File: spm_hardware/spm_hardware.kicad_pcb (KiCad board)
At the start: 2 copper layers, 108 x 81 mm, 76 parts, among them J1 Magnet sensor, J2 Floater, J3 MotIn, J4 MotOut, J5 230VAC, J6 USonic sensor, J7 Temp&Humid sensor, J8 Flow sensor, J9 HAL sensor, P1 DIL6, P2 DIL6, P3 DIL6, P4 CONN_01X02, P5 CONN_01X02, P6 CONN_01X02, P7 CONN_01X02, Q1 BS170, Q2 Q_NMOS_DGS, Q3 Q_NMOS_DGS, Q4 Q_NMOS_DGS, T1 Transformer_1P_1S, U1 G3MB-202P, U2 ESP-12E, U3 STM32L432, U4 LTV-817, U5 LTV-817

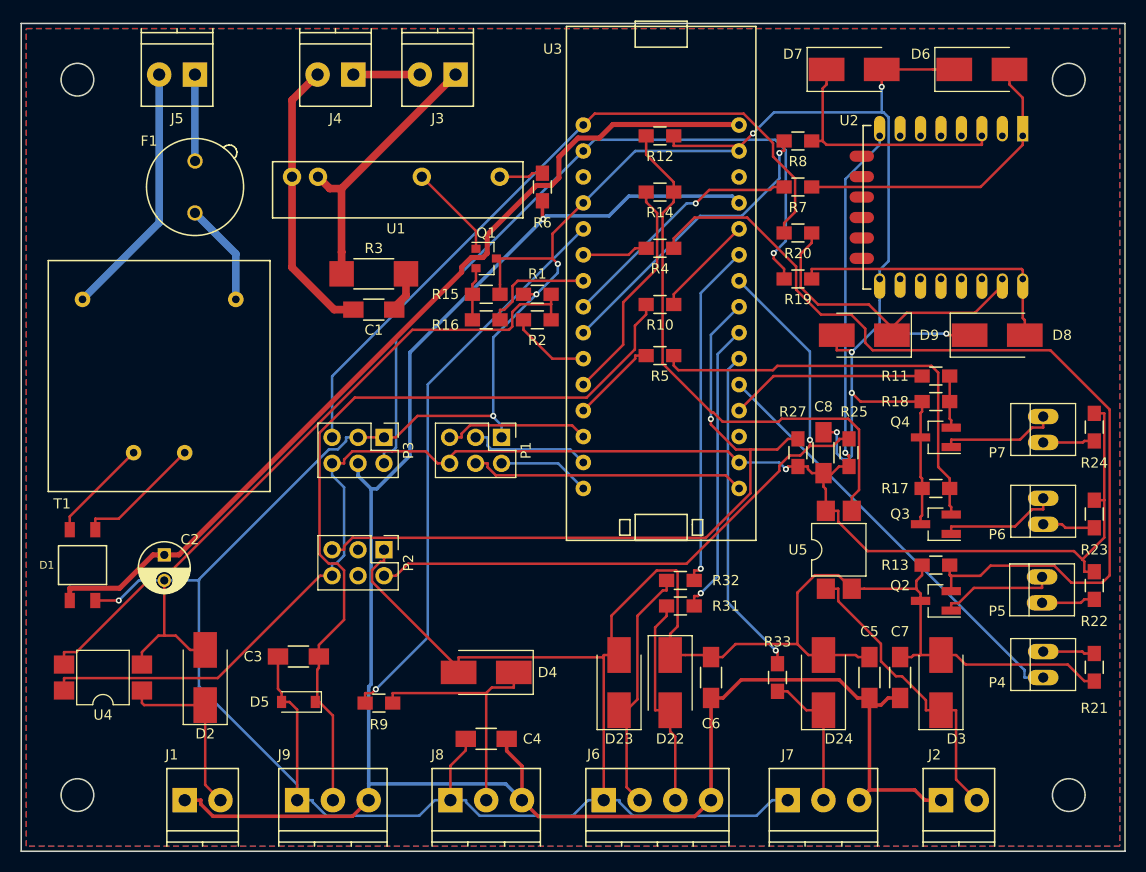
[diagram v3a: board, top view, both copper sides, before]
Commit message: Change UART pins and improve PCB layout
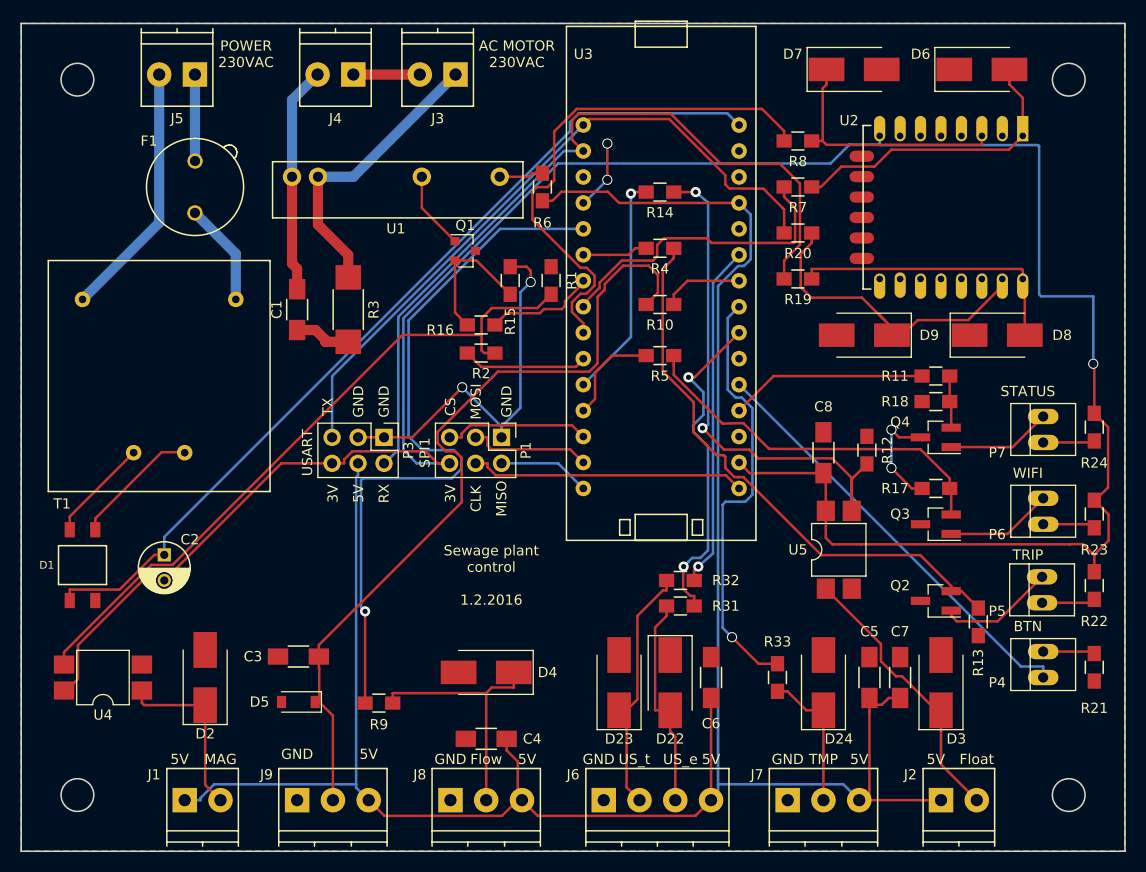
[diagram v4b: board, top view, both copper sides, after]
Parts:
- removed P2: DIL6, Pin_Headers:Pin_Header_Straight_2x03_Pitch2.54mm
- removed R25, R27: R, Resistors_SMD:R_0805_HandSoldering
- moved R12 36.8 mm to (160.7, 90.1), turned to 90 degrees
- moved C1 7.50 mm to (105.0, 76.4), turned to 90 degrees
- moved R13 6.93 mm to (171.6, 106.9), turned to 90 degrees
- moved R2 6.39 mm to (123.0, 80.6)
- moved R3 4.30 mm to (110.0, 76.4), turned to 90 degrees
- moved R15 2.71 mm to (125.8, 73.5), turned to 90 degrees
- moved Q1 2.18 mm to (121.4, 70.6)
- moved R1 1.91 mm to (129.8, 73.5), turned to 90 degrees
- moved R16 0.71 mm to (123.0, 77.9)
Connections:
- U3 pad 20: HAL_Sen -> (no net)
- U3 pad 22: I2C_CLK -> HAL_Sen
- U3 pad 23: I2C_SDA -> TH_Sensor
- U3 pad 25: TH_Sensor -> (no net)
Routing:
- net GND: track 457.8 -> 55.0 mm, vias 10 -> 6
- net I2C_CLK: track 70.4 -> 0.00 mm, vias 1 -> 0
- net I2C_SDA: track 70.3 -> 0.00 mm, vias 1 -> 0
- net +3V3: track 183.1 -> 229.8 mm, vias 2 -> 1
- net Net-(Q2-Pad2): track 90.2 -> 55.6 mm
- net WIFI_EN: track 29.5 -> 51.0 mm, vias 1 -> 0
- net +5V: track 199.2 -> 220.2 mm, vias 1 -> 0
- net Flow_Sen: track 55.6 -> 71.6 mm
- net TH_Sensor: track 32.3 -> 42.5 mm
- net Net-(Q1-Pad2): track 5.19 -> 13.6 mm
- net WIFI_RST: track 24.5 -> 30.7 mm, vias 1 -> 0
- net Net-(C1-Pad2): track 27.6 -> 22.2 mm
- net USART1_RX: track 73.3 -> 78.6 mm, vias 1 -> 0
- net Net-(Q3-Pad2): track 41.9 -> 36.7 mm
- net Mag_Sw: track 8.00 -> 12.3 mm
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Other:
- net class 12V: trace_width 0.5 -> 0.25; via_dia 0.6 -> 1; via_drill 0.4 -> 0.8
- net class 230V: trace_width 0.75 -> 1; via_dia 1.2 -> 1.4; via_drill 0.5 -> 1.2
- net class 5V: trace_width 0.35 -> 0.25; via_dia 0.6 -> 1; via_drill 0.4 -> 0.8
- net class Default: via_dia 0.6 -> 1; via_drill 0.4 -> 0.8
- board text added: "3V"
- board text added: "5V"
- board text added: "AC MOTOR 230VAC"
- board text added: "BTN"
- board text added: "CLK"
- board text added: "CS"
- board text added: "Float"
- board text added: "Flow"
- board text added: "GND"
- board text added: "MAG"
- board text added: "MISO"
- board text added: "MOSI"
- board text added: "POWER 230VAC"
- board text added: "RX"
- board text added: "SPI1"
- board text added: "STATUS"
- board text added: "Sewage plant control 1.2.2016"
- board text added: "TMP"
- board text added: "TRIP"
- board text added: "TX"
- board text added: "USART"
- board text added: "US_e"
- board text added: "US_t"
- board text added: "WIFI"

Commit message: PCB design improved
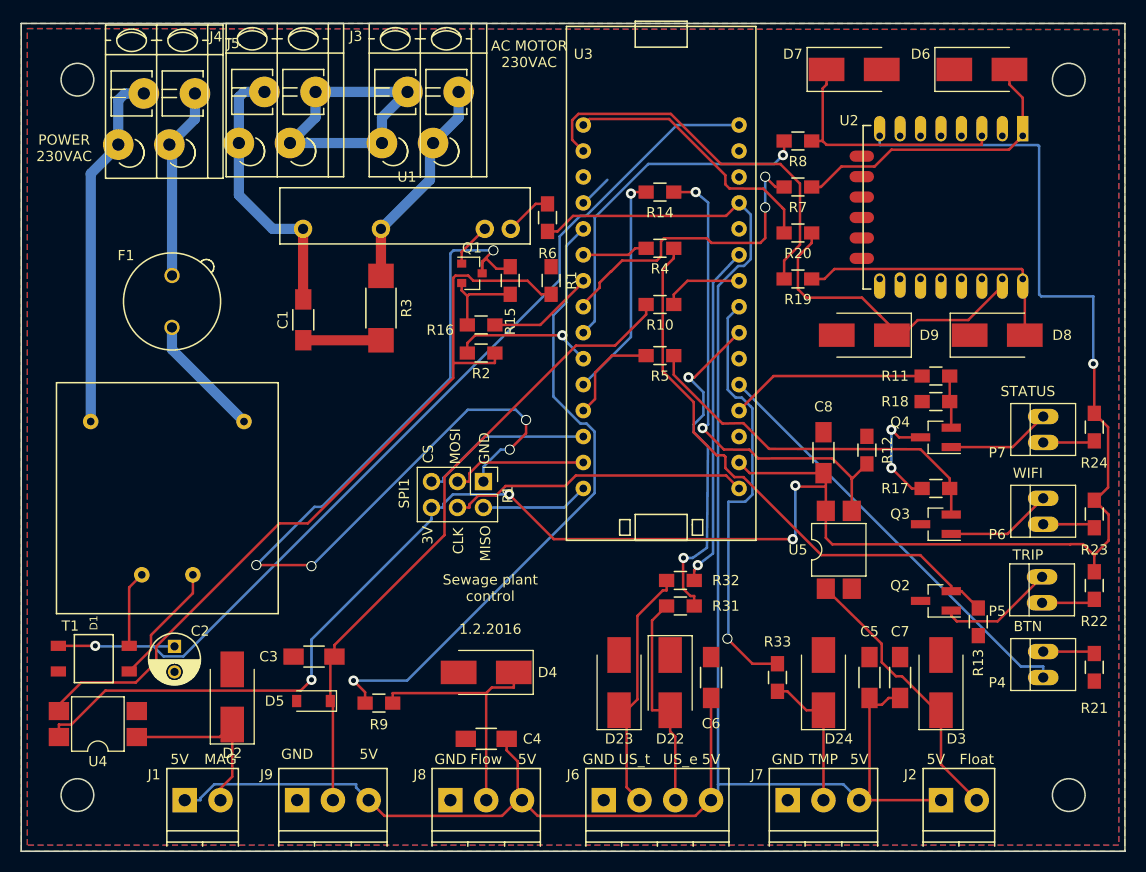
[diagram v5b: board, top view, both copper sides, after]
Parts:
- removed P3: DIL6, Pin_Headers:Pin_Header_Straight_2x03_Pitch2.54mm
- J3, J4, J5: footprint Connectors_Terminal_Blocks:TerminalBlock_Pheonix_PT-3.5mm_2pol -> Connectors_Terminal_Blocks:TerminalBlock_WAGO-804_RM5mm_2pol
- moved U1 22.0 mm to (125.9, 68.5), turned to 180 degrees
- moved T1 12.0 mm to (99.8, 87.3)
- moved F1 11.4 mm to (92.7, 75.6)
- moved D1 9.22 mm to (85.1, 110.5), turned to 270 degrees
- moved C2 9.01 mm to (93.0, 109.3)
- moved P1 4.68 mm to (123.2, 93.2)
- moved U4 4.58 mm to (85.5, 116.9)
- moved J4 4.07 mm to (106.8, 55.1)
- moved D2 3.26 mm to (98.6, 114.3)
- moved R3 3.20 mm to (113.2, 76.2)
- moved R6 3.04 mm to (129.5, 67.4)
- moved Q1 2.29 mm to (122.1, 72.8)
- moved J5 1.85 mm to (95.0, 55.2)
- moved J3 1.73 mm to (120.8, 55.1)
- moved C3 1.53 mm to (106.6, 110.3)
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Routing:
- net GND: track 55.0 -> 105.8 mm, vias 6 -> 7
- net USART1_TX: track 67.1 -> 26.4 mm
- net USART1_RX: track 78.6 -> 38.8 mm
- net +5V: track 220.2 -> 188.6 mm
- net +3V3: track 229.8 -> 203.8 mm, vias 1 -> 5
- net Net-(J3-Pad2): track 6.50 -> 30.1 mm
- net WIFI_EN: track 51.0 -> 34.1 mm, vias 0 -> 1
- net Net-(C3-Pad1): track 80.5 -> 63.6 mm
- net Net-(R1-Pad1): track 67.3 -> 78.6 mm
- net Net-(F1-Pad2): track 8.46 -> 18.7 mm
- net Net-(J5-Pad2): track 25.1 -> 35.3 mm
- net Flow_Sen: track 71.6 -> 62.9 mm
- net Net-(J3-Pad1): track 28.7 -> 21.1 mm
- net +12V: track 87.9 -> 93.1 mm, vias 0 -> 1
- net Net-(Q1-Pad2): track 13.6 -> 8.60 mm
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- added copper zone on B.Cu, net (none)
- added copper zone on F.Cu, net (none)
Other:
- board text removed: "RX"
- board text removed: "TX"
- board text removed: "USART"

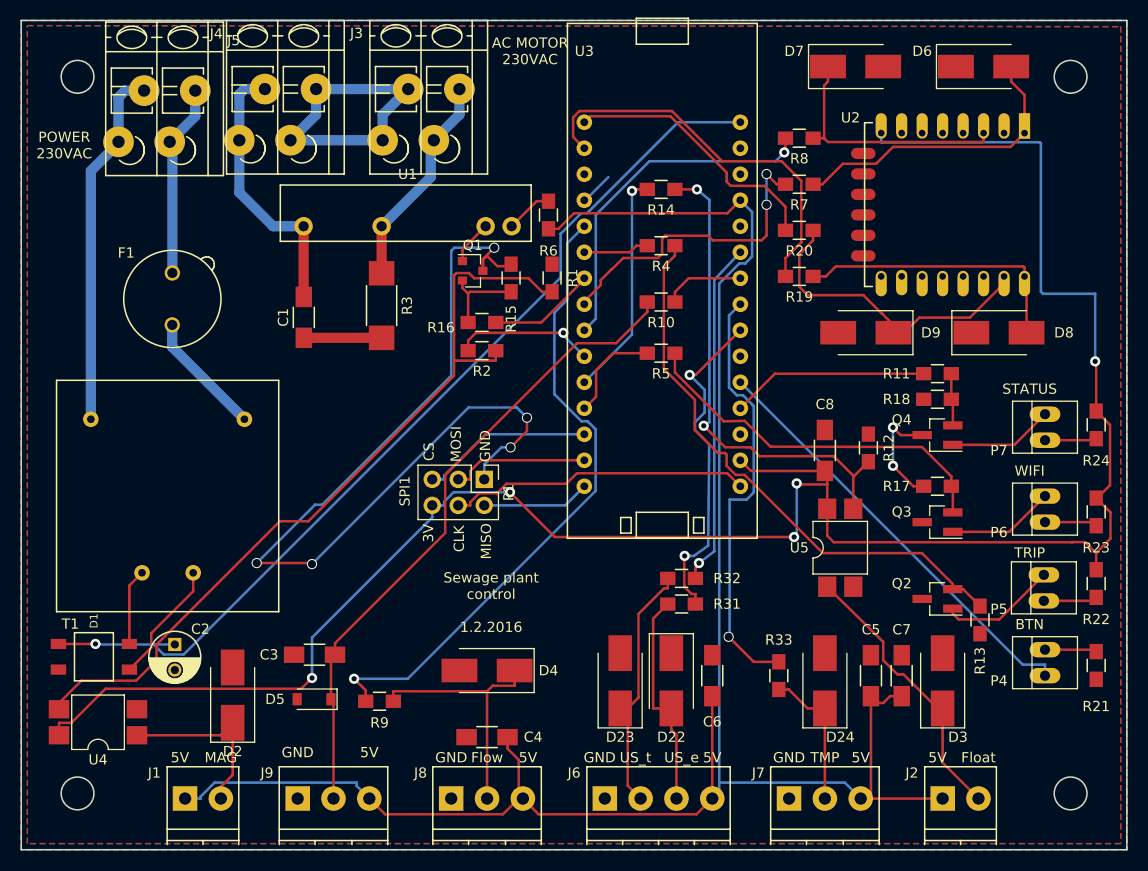
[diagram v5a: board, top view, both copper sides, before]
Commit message: Add custom vias and apply on PCB
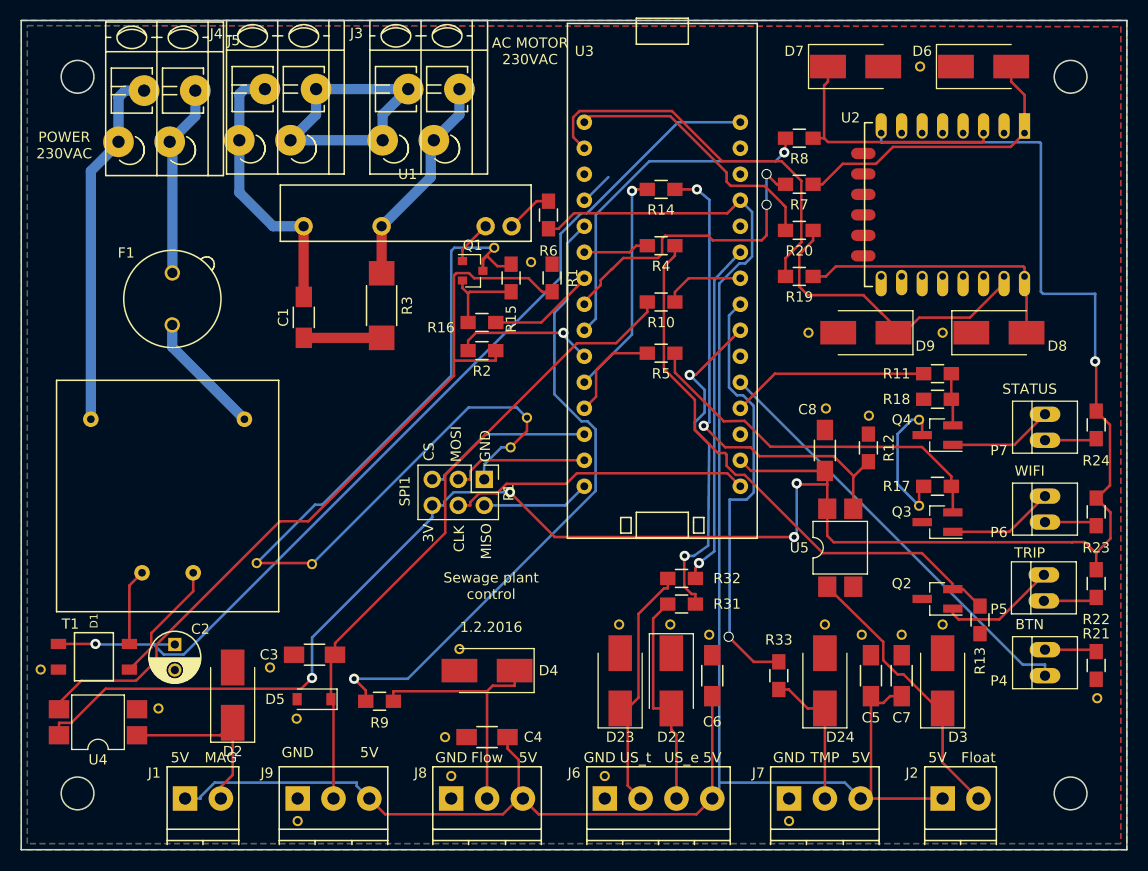
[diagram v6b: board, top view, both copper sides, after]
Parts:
- added ?: via-0.6, vias:via-0.6, F.Cu at (165.8, 52.9)
- added ?: via-0.6, vias:via-0.6, F.Cu at (164.0, 108.4)
- added ?: via-0.6, vias:via-0.6, F.Cu at (160.1, 108.4)
- added ?: via-0.6, vias:via-0.6, F.Cu at (156.5, 107.4)
- added ?: via-0.6, vias:via-0.6, F.Cu at (102.3, 111.6)
- added ?: via-0.6, vias:via-0.6, F.Cu at (104.9, 116.6)
- added ?: via-0.6, vias:via-0.6, F.Cu at (79.9, 111.8)
- added ?: via-0.6, vias:via-0.6, F.Cu at (91.4, 115.6)
- added ?: via-0.6, vias:via-0.6, F.Cu at (120.8, 109.8)
- added ?: via-0.6, vias:via-0.6, F.Cu at (101.0, 101.4)
- added ?: via-0.6, vias:via-0.6, F.Cu at (106.4, 101.5)
- added ?: via-0.6, vias:via-0.6, F.Cu at (168.0, 78.9)
- added ?: via-0.6, vias:via-0.6, F.Cu at (127.4, 87.2)
- added ?: via-0.6, vias:via-0.6, F.Cu at (125.8, 90.1)
- added ?: via-0.6, vias:via-0.6, F.Cu at (153.0, 126.6)
- added ?: via-0.6, vias:via-0.6, F.Cu at (135.0, 122.2)
- added ?: via-0.6, vias:via-0.6, F.Cu at (145.2, 108.4)
- added ?: via-0.6, vias:via-0.6, F.Cu at (119.4, 118.4)
- added ?: via-0.6, vias:via-0.6, F.Cu at (141.4, 107.4)
- added ?: via-0.6, vias:via-0.6, F.Cu at (136.4, 107.4)
- added ?: via-0.6, vias:via-0.6, F.Cu at (120.0, 122.2)
- added ?: via-0.6, vias:via-0.6, F.Cu at (105.0, 126.6)
- added ?: via-0.6, vias:via-0.6, F.Cu at (154.9, 78.9)
- added ?: via-0.6, vias:via-0.6, F.Cu at (124.2, 70.6)
- added ?: via-0.6, vias:via-0.6, F.Cu at (127.8, 72.0)
- added ?: via-0.4, vias:via-0.4, F.Cu at (127.8, 72.4)
- added ?: via-0.6, vias:via-0.6, F.Cu at (156.6, 86.3)
- added ?: via-0.6, vias:via-0.6, F.Cu at (160.8, 87.0)
- added ?: via-0.6, vias:via-0.6, F.Cu at (165.7, 87.4)
- added ?: via-0.6, vias:via-0.6, F.Cu at (165.7, 95.8)
- added ?: via-0.6, vias:via-0.6, F.Cu at (183.1, 114.6)
- added ?: via-0.6, vias:via-0.6, F.Cu at (168.0, 107.4)
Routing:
- net GND: track 105.8 -> 104.1 mm, vias 7 -> 0
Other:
- net class 12V: via_drill 0.8 -> 0.6
- net class 230V: via_drill 1.2 -> 1
- net class 5V: via_drill 0.8 -> 0.6
- net class Default: via_drill 0.8 -> 0.6
